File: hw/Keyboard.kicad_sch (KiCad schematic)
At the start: 19 parts, among them J1000 USB-61400416121, J1001 FC68125, J1002 FC68125, J1003 FC68125, J2000 FC68125, J3000 FC68125, J4000 FC68125, X1 Audio_Cable_3.5mm_4Pin, X2 Audio_Cable_3.5mm_4Pin, X3 Audio_Cable_3.5mm_4Pin

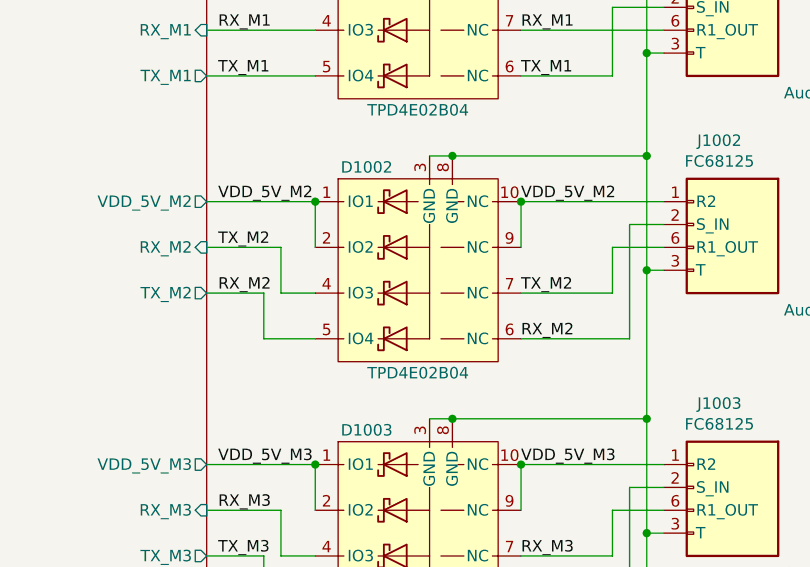
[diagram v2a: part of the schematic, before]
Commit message: Add pull-downs to power switches.
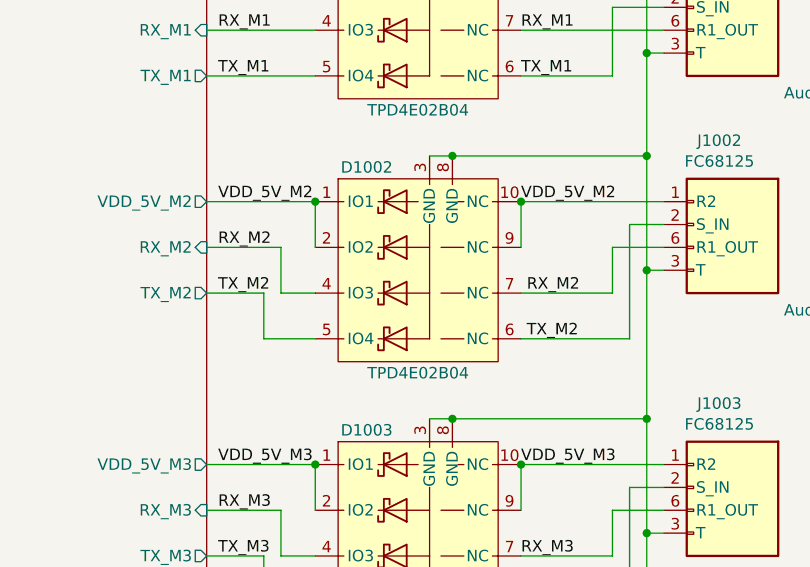
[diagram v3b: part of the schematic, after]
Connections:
- net RX_M2: now also D1002.4 (IO3), D1002.7 (NC), J1002.6 (R1); no longer D1002.5 (IO4), D1002.6 (NC), J1002.2 (S)
- net TX_M2: now also D1002.5 (IO4), D1002.6 (NC), J1002.2 (S); no longer D1002.4 (IO3), D1002.7 (NC), J1002.6 (R1)
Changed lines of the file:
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@@
     (effects (font (size 1.27 1.27)) (justify left bottom))
   )
-  (label "TX_M2" (at 131.445 97.79 0)
+  (label "TX_M2" (at 132.08 102.87 0)
     (effects (font (size 1.27 1.27)) (justify left bottom))
   )
@@
     (effects (font (size 1.27 1.27)) (justify left bottom))
   )
-  (label "RX_M2" (at 97.79 97.79 0)
+  (label "RX_M2" (at 97.79 92.71 0)
     (effects (font (size 1.27 1.27)) (justify left bottom))
   )
@@
     (effects (font (size 1.27 1.27)) (justify left bottom))
   )
-  (label "RX_M2" (at 131.445 102.87 0)
+  (label "RX_M2" (at 132.08 97.79 0)
     (effects (font (size 1.27 1.27)) (justify left bottom))
   )
@@
     (effects (font (size 1.27 1.27)) (justify left bottom))
   )
-  (label "TX_M2" (at 97.79 92.71 0)
+  (label "TX_M2" (at 97.79 97.79 0)
     (effects (font (size 1.27 1.27)) (justify left bottom))
   )
@@
       (reference "R1201") (unit 1) (value "22.6kR") (footprint "Keyboard:R_0402")
     )
+    (path "/00000000-0000-0000-0000-00005efb9ff1/00000000-0000-0000-0000-00005f11f966/2a78a64a-aa6b-411d-9021-ef1aec0645a2"
+      (reference "R1202") (unit 1) (value "10.0kR") (footprint "Keyboard:R_0402")
+    )
+    (path "/00000000-0000-0000-0000-00005efb9ff1/00000000-0000-0000-0000-00005f11f966/dd507a1e-1ac3-4988-b0e6-879a64d1ef7e"
+      (reference "R1203") (unit 1) (value "10.0kR") (footprint "Keyboard:R_0402")
+    )
+    (path "/00000000-0000-0000-0000-00005efb9ff1/00000000-0000-0000-0000-00005f11f966/3b6246af-edb1-4d12-b8e0-2438f54cb5b9"
+      (reference "R1204") (unit 1) (value "10.0kR") (footprint "Keyboard:R_0402")
+    )
     (path "/00000000-0000-0000-0000-00005efb9ff1/00000000-0000-0000-0000-00005f163059/7e3cda1f-4757-4889-9afa-473cee754858"
